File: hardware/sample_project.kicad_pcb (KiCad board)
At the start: 2 copper layers, 43.2 x 43.2 mm, 3 parts

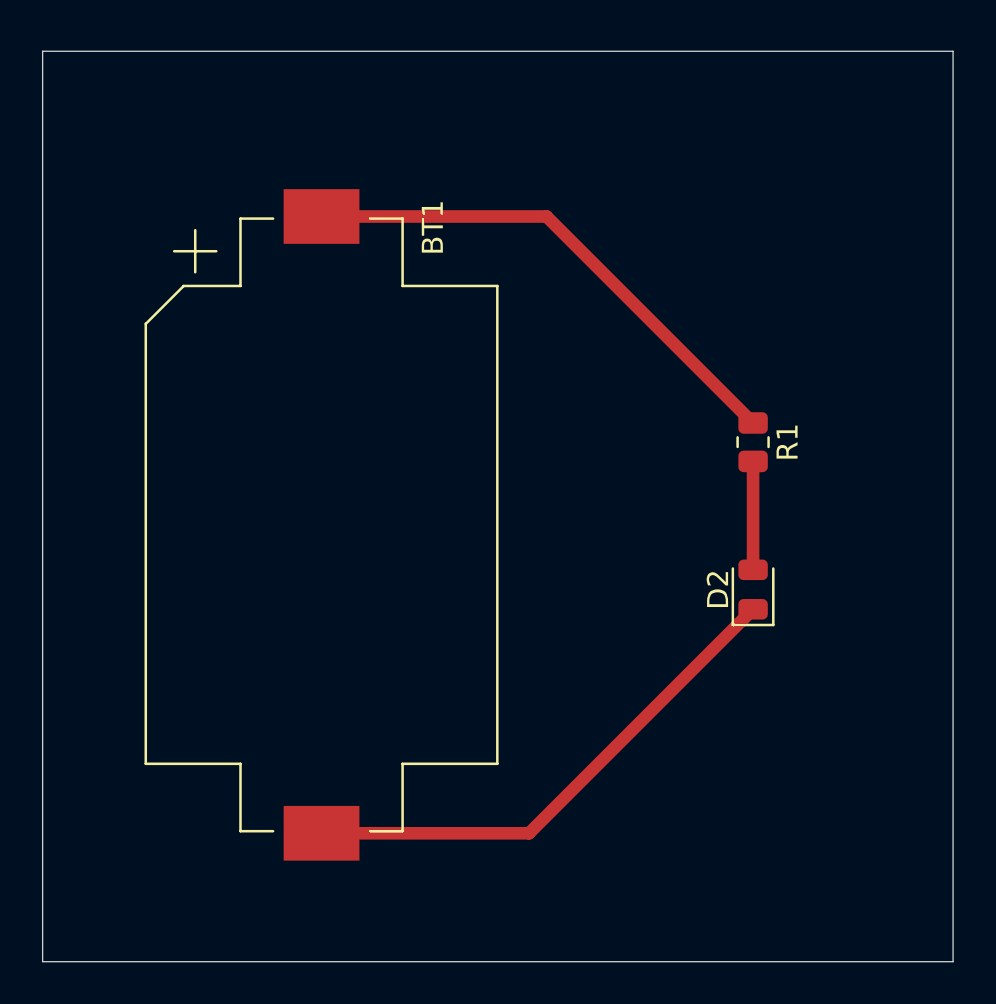
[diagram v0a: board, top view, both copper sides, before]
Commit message: added positions and 3D model
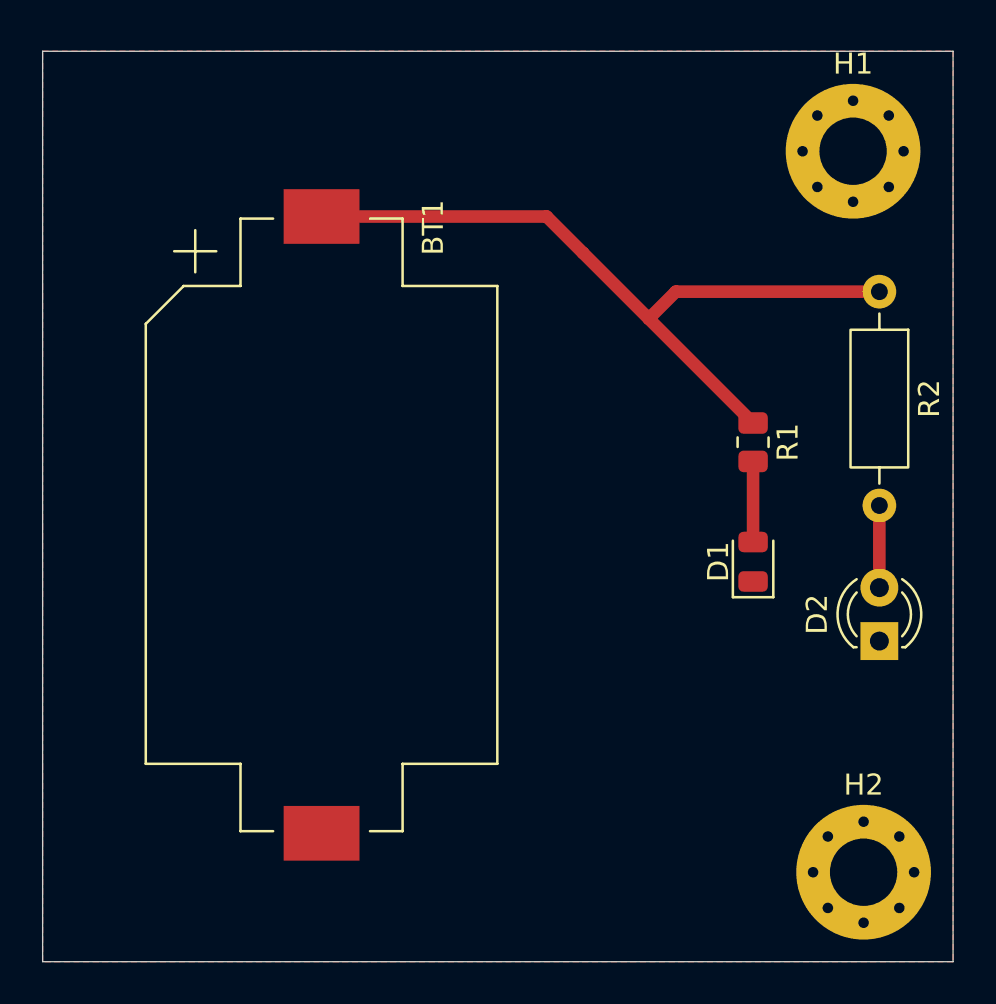
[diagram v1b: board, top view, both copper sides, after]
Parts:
- added D1: LED_Small, LED_SMD:LED_0805_2012Metric, F.Cu at (140.2, 110.5)
- added H1: MountingHole_Pad, MountingHole:MountingHole_3.2mm_M3_Pad_Via, F.Cu at (145.0, 91.0)
- added H2: MountingHole_Pad, MountingHole:MountingHole_3.2mm_M3_Pad_Via, F.Cu at (145.5, 125.2)
- added R2: R_Small, Resistor_THT:R_Axial_DIN0207_L6.3mm_D2.5mm_P10.16mm_Horizontal, F.Cu at (146.2, 97.7)
- D2: footprint LED_SMD:LED_0805_2012Metric -> LED_THT:LED_D3.0mm
- moved D2 6.48 mm to (146.2, 114.3)
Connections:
- R1 pad 2: Net-(D2-A) -> Net-(D1-A)
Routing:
- net GND: track 24.9 -> 0.00 mm
- net +BATT: track 24.6 -> 36.0 mm
- net Net-(D1-A): track 0.00 -> 3.83 mm
- net Net-(D2-A): track 5.15 -> 3.90 mm
- added copper zone on F.Cu, net GND
